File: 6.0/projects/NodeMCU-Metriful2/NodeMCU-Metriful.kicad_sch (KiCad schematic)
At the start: 20 parts, among them CN1 RJ10, CN2 RJ10, CN3 RJ10, J1 Conn_02x04_Odd_Even, J4 Conn_01x03_Female, Q1 BSS138BKW, Q2 NX2301P, U1 NodeMCU_1.0_(ESP-12E), U2 Metriful-1, U3 DS18B20

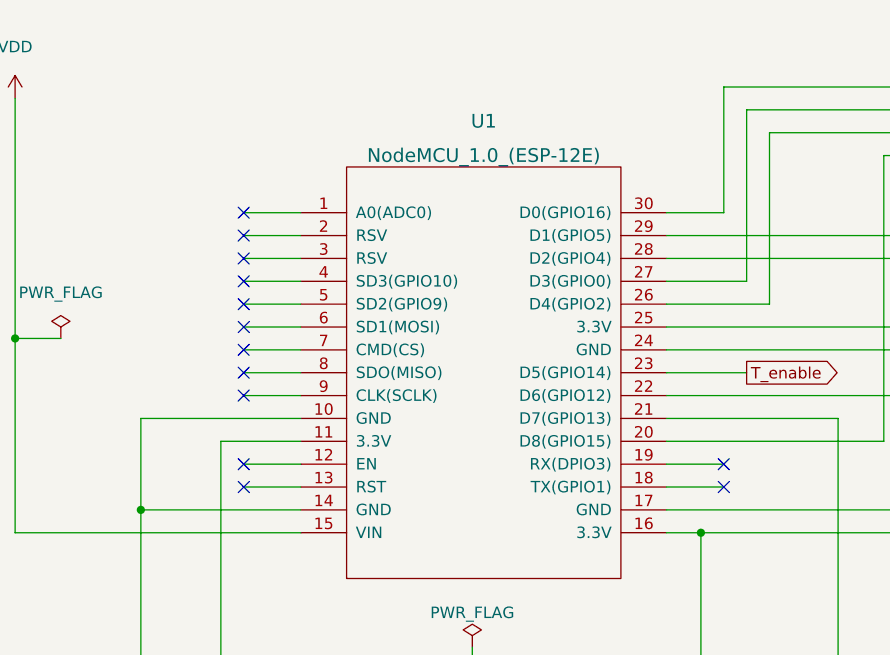
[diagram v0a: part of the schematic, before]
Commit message: Add header, move components to the left to make room for deep-sleep pin header
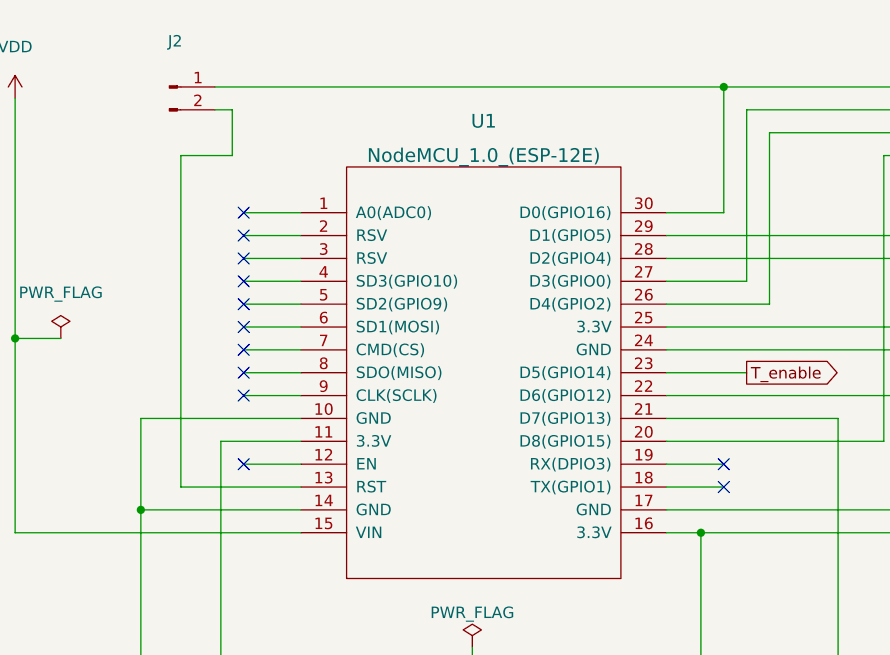
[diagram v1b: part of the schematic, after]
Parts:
- added J2: (no value), symbol Connector:Conn_01x02_Male
- U1: footprint (none) -> NodeMCU:NodeMCU_0.1_Axel
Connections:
- net at U1.13 (RST): now also J2.2 (Pin_2)
- net at J1.1 (Pin_1), U1.30 (D0(GPIO16)): now also J2.1 (Pin_1)
- no-connect marks 19 -> 18
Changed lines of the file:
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@@
   (junction (at 135.89 24.13) (diameter 0) (color 0 0 0 0)
+  )
+  (junction (at 100.33 24.13) (diameter 0) (color 0 0 0 0)
   )
   (junction (at 214.63 132.08) (diameter 0) (color 0 0 0 0)
@@
   (no_connect (at 46.99 58.42))
   (no_connect (at 46.99 66.04))
-  (no_connect (at 46.99 68.58))
   (no_connect (at 217.17 108.585))
   (no_connect (at 198.12 108.585))
@@
     (stroke (width 0) (type default) (color 0 0 0 0))
   )
+  (wire (pts (xy 40.005 31.75) (xy 40.005 68.58))
+    (stroke (width 0) (type default) (color 0 0 0 0))
+  )
   (wire (pts (xy 93.98 38.1) (xy 100.33 38.1))
     (stroke (width 0) (type default) (color 0 0 0 0))
@@
     (stroke (width 0) (type default) (color 0 0 0 0))
   )
+  (wire (pts (xy 43.815 26.67) (xy 45.72 26.67))
+    (stroke (width 0) (type default) (color 0 0 0 0))
+  )
   (wire (pts (xy 46.99 40.64) (xy 53.34 40.64))
     (stroke (width 0) (type default) (color 0 0 0 0))
@@
     (stroke (width 0) (type default) (color 0 0 0 0))
   )
+  (wire (pts (xy 45.72 26.67) (xy 45.72 31.75))
+    (stroke (width 0) (type default) (color 0 0 0 0))
+  )
   (wire (pts (xy 80.645 138.43) (xy 72.39 138.43))
     (stroke (width 0) (type default) (color 0 0 0 0))
@@
     (stroke (width 0) (type default) (color 0 0 0 0))
   )
+  (wire (pts (xy 43.815 24.13) (xy 100.33 24.13))
+    (stroke (width 0) (type default) (color 0 0 0 0))
+  )
   (wire (pts (xy 121.92 53.34) (xy 121.92 71.12))
     (stroke (width 0) (type default) (color 0 0 0 0))
   )
+  (wire (pts (xy 45.72 31.75) (xy 40.005 31.75))
+    (stroke (width 0) (type default) (color 0 0 0 0))
+  )
   (wire (pts (xy 80.01 149.86) (xy 92.71 149.86))
     (stroke (width 0) (type default) (color 0 0 0 0))
@@
     (stroke (width 0) (type default) (color 0 0 0 0))
   )
-  (wire (pts (xy 46.99 68.58) (xy 53.34 68.58))
+  (wire (pts (xy 40.005 68.58) (xy 53.34 68.58))
     (stroke (width 0) (type default) (color 0 0 0 0))
   )
@@
       (effects (font (size 1.524 1.524)))
     )
-    (property "Footprint" "" (id 2) (at 58.42 77.47 0)
+    (property "Footprint" "NodeMCU:NodeMCU_0.1_Axel" (id 2) (at 58.42 77.47 0)
       (effects (font (size 1.524 1.524)) hide)
     )
@@
     (pin "1")
   )
+  (symbol (lib_id "Connector:Conn_01x02_Male") (at 38.735 24.13 0) (unit 1)
+    (in_bom yes) (on_board yes) (fields_autoplaced)
+    (property "Reference" "J2" (id 0) (at 39.37 19.05 0))
+    (property "Value" "" (id 1) (at 39.37 21.59 0))
+    (property "Footprint" "" (id 2) (at 38.735 24.13 0)
+      (effects (font (size 1.27 1.27)) hide)
+    )
+    (property "Datasheet" "~" (id 3) (at 38.735 24.13 0)
+      (effects (font (size 1.27 1.27)) hide)
+    )
+    (pin "1")
+    (pin "2")
+  )
   (sheet_instances
     (path "/" (page "1"))
@@
       (reference "J1") (unit 1) (value "Conn_02x04_Odd_Even") (footprint "Connector_PinHeader_2.54mm:PinHeader_2x04_P2.54mm_Vertical")
     )
+    (path "/fd878e0c-0f76-4a79-b706-cc183d4afca9"
+      (reference "J2") (unit 1) (value "Deep Sleep") (footprint "Connector_PinHeader_2.54mm:PinHeader_1x02_P2.54mm_Vertical")
+    )
     (path "/aebbb1f6-af4a-4db4-86ab-be1d87eefd03"

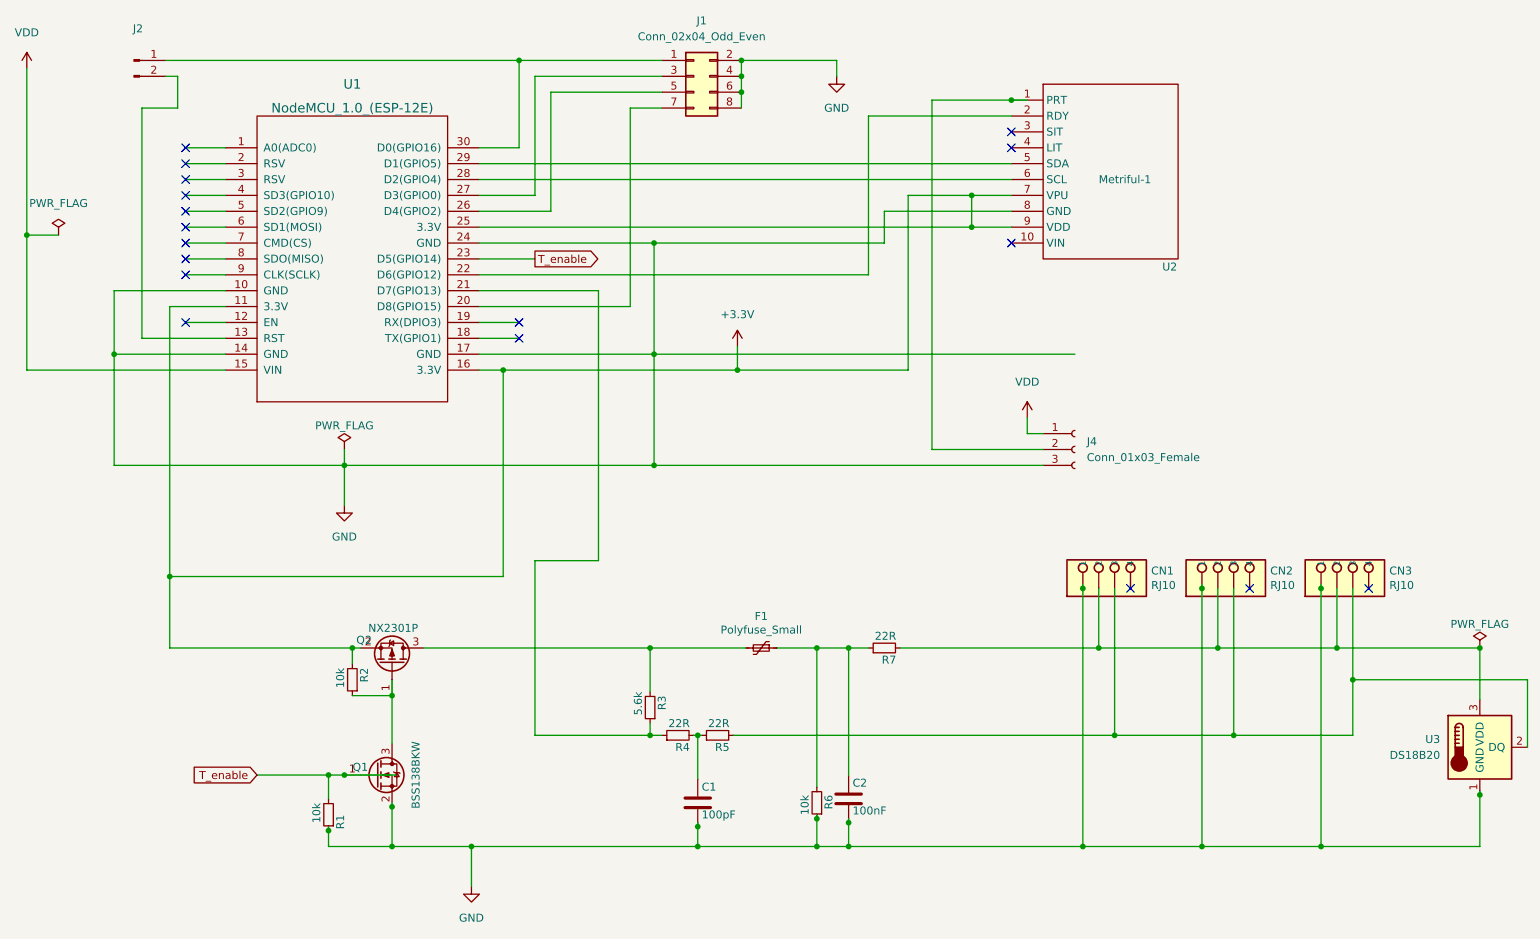
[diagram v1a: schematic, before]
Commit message: Many last-minute changes, mostly to silkscreen and some positioning
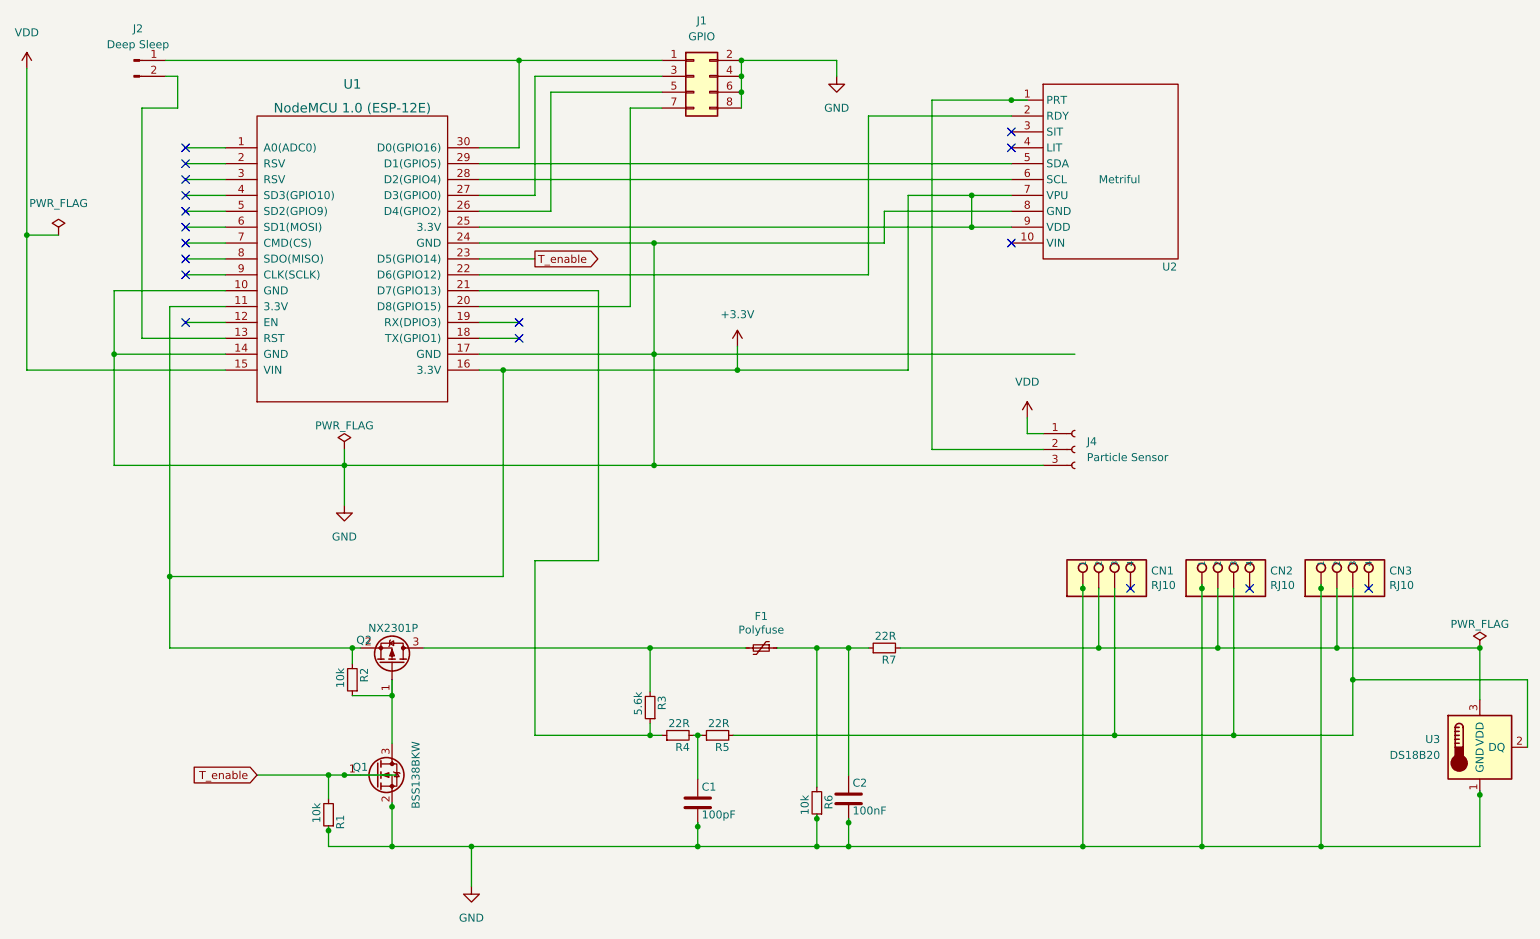
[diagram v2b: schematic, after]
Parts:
- F1: value Polyfuse_Small -> Polyfuse
- J1: value Conn_02x04_Odd_Even -> GPIO
- J2: value (none) -> Deep Sleep; footprint (none) -> Connector_PinHeader_2.54mm:PinHeader_1x02_P2.54mm_Vertical
- J4: value Conn_01x03_Female -> Particle Sensor
- U1: value NodeMCU_1.0_(ESP-12E) -> NodeMCU 1.0 (ESP-12E)
- U2: value Metriful-1 -> Metriful
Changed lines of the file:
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@@
       (effects (font (size 1.524 1.524)))
     )
-    (property "Value" "NodeMCU_1.0_(ESP-12E)" (id 1) (at 73.66 31.75 0)
+    (property "Value" "NodeMCU 1.0 (ESP-12E)" (id 1) (at 73.66 31.75 0)
       (effects (font (size 1.524 1.524)))
     )
@@
       (effects (font (size 1.27 1.27)) (justify left))
     )
-    (property "Value" "Metriful-1" (id 1) (at 193.04 43.18 0)
+    (property "Value" "Metriful" (id 1) (at 193.04 43.18 0)
       (effects (font (size 1.27 1.27)) (justify left))
     )
@@
       (effects (font (size 1.27 1.27)) (justify left))
     )
-    (property "Value" "Conn_01x03_Female" (id 1) (at 191.135 87.6299 0)
+    (property "Value" "Particle Sensor" (id 1) (at 191.135 87.6299 0)
       (effects (font (size 1.27 1.27)) (justify left))
     )
@@
     (in_bom yes) (on_board yes)
     (property "Reference" "F1" (id 0) (at 139.065 113.03 90))
-    (property "Value" "Polyfuse_Small" (id 1) (at 139.065 115.2144 90))
+    (property "Value" "Polyfuse" (id 1) (at 139.065 115.2144 90))
     (property "Footprint" "Fuse:Fuse_1210_3225Metric_Pad1.42x2.65mm_HandSolder" (id 2) (at 133.985 119.38 0)
       (effects (font (size 1.27 1.27)) (justify left) hide)
@@
     (in_bom yes) (on_board yes) (fields_autoplaced)
     (property "Reference" "J1" (id 0) (at 129.54 17.78 0))
-    (property "Value" "Conn_02x04_Odd_Even" (id 1) (at 129.54 20.32 0))
+    (property "Value" "GPIO" (id 1) (at 129.54 20.32 0))
     (property "Footprint" "Connector_PinHeader_2.54mm:PinHeader_2x04_P2.54mm_Vertical" (id 2) (at 128.27 26.67 0)
       (effects (font (size 1.27 1.27)) hide)
@@
     (in_bom yes) (on_board yes) (fields_autoplaced)
     (property "Reference" "J2" (id 0) (at 39.37 19.05 0))
-    (property "Value" "" (id 1) (at 39.37 21.59 0))
-    (property "Footprint" "" (id 2) (at 38.735 24.13 0)
+    (property "Value" "Deep Sleep" (id 1) (at 39.37 21.59 0))
+    (property "Footprint" "Connector_PinHeader_2.54mm:PinHeader_1x02_P2.54mm_Vertical" (id 2) (at 38.735 24.13 0)
       (effects (font (size 1.27 1.27)) hide)
     )
@@
     )
     (path "/b6440db5-483d-4340-bc00-e7165ccde6b3"
-      (reference "F1") (unit 1) (value "Polyfuse_Small") (footprint "Fuse:Fuse_1210_3225Metric_Pad1.42x2.65mm_HandSolder")
+      (reference "F1") (unit 1) (value "Polyfuse") (footprint "Fuse:Fuse_1210_3225Metric_Pad1.42x2.65mm_HandSolder")
     )
     (path "/ce89592b-25ef-4249-9dbd-039fc52a7c45"
-      (reference "J1") (unit 1) (value "Conn_02x04_Odd_Even") (footprint "Connector_PinHeader_2.54mm:PinHeader_2x04_P2.54mm_Vertical")
+      (reference "J1") (unit 1) (value "GPIO") (footprint "Connector_PinHeader_2.54mm:PinHeader_2x04_P2.54mm_Vertical")
     )
     (path "/fd878e0c-0f76-4a79-b706-cc183d4afca9"
@@
     )
     (path "/aebbb1f6-af4a-4db4-86ab-be1d87eefd03"
-      (reference "J4") (unit 1) (value "Conn_01x03_Female") (footprint "Connector_JST:JST_PH_B3B-PH-K_1x03_P2.00mm_Vertical")
+      (reference "J4") (unit 1) (value "Particle Sensor") (footprint "Connector_JST:JST_PH_B3B-PH-K_1x03_P2.00mm_Vertical")
     )
     (path "/2b586e14-22cd-4c20-8969-51f54accd3f7"
@@
     )
     (path "/4aa6fb68-a1f5-4b50-b82f-f651e01496b4"
-      (reference "U1") (unit 1) (value "NodeMCU_1.0_(ESP-12E)") (footprint "NodeMCU:NodeMCU_0.1_Axel")
+      (reference "U1") (unit 1) (value "NodeMCU 1.0 (ESP-12E)") (footprint "NodeMCU:NodeMCU_0.1_Axel")
     )
     (path "/51cc007a-3378-4ce3-909c-71e94822f8d1"
-      (reference "U2") (unit 1) (value "Metriful-1") (footprint "Sensor:Metriful-1")
+      (reference "U2") (unit 1) (value "Metriful") (footprint "Sensor:Metriful-1")
     )
     (path "/d579d5d9-9b2f-4342-8d74-45e2b972dab4"
